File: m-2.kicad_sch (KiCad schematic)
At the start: 57 parts, among them J1 2199230-6, J2 1-2199230-6, M2 M2_4222, M3 M2_2280, U2 74LVC2G07GV, U3 74LVC2G07GV, Y1 ECS-327MVATX-2-CN-TR3

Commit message: Loclib
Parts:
- C10, C13, C14, C15, C16, C17, C18, C19, C20, C9: footprint antmicro-footprints:0402-cap -> jetson-orin-baseboard-footprints:0402-cap; symbol antmicroCapacitors0402:C_220n_0402 -> jetson-orin-baseboard:C_220n_0402
- C11, C12, C21, C22, C23, C24: footprint antmicro-footprints:0603-cap -> jetson-orin-baseboard-footprints:0603-cap; symbol antmicroCapacitors0603:C_10u_0603 -> jetson-orin-baseboard:C_10u_0603
- C25, C7, C8: footprint antmicro-footprints:0402-cap -> jetson-orin-baseboard-footprints:0402-cap; symbol antmicroCapacitors0402:C_100n_0402 -> jetson-orin-baseboard:C_100n_0402
- D1: footprint antmicro-footprints:LED_0603 -> jetson-orin-baseboard-footprints:LED_0603; symbol antmicroLEDIndicationDiscrete:LTST-C190GKT -> jetson-orin-baseboard:LTST-C190GKT
- J1: footprint antmicro-footprints:2199230-4 -> jetson-orin-baseboard-footprints:2199230-4; symbol antmicroPciConnectors:2199230-6 -> jetson-orin-baseboard:2199230-6
- J2: footprint antmicro-footprints:1-2199230-6 -> jetson-orin-baseboard-footprints:1-2199230-6; symbol antmicroPciConnectors:1-2199230-6 -> jetson-orin-baseboard:1-2199230-6
- M2: footprint antmicro-footprints:m2_4222 -> jetson-orin-baseboard-footprints:m2_4222; symbol antmicroModules:M2_4222 -> jetson-orin-baseboard:M2_4222
- M3: footprint antmicro-footprints:m2_2280 -> jetson-orin-baseboard-footprints:m2_2280; symbol antmicroModules:M2_2280 -> jetson-orin-baseboard:M2_2280
- R13, R14, R15, R16, R17, R18, R19, R20, R29, R30, R31, R52: footprint antmicro-footprints:0402-res -> jetson-orin-baseboard-footprints:0402-res; symbol antmicroResistors0402:R_0R_0402 -> jetson-orin-baseboard:R_0R_0402
- R143: footprint antmicro-footprints:0805-res -> jetson-orin-baseboard-footprints:0805-res; symbol antmicroResistorsmisc:R_0R_0805 -> jetson-orin-baseboard:R_0R_0805
- R21, R22: footprint antmicro-footprints:EXB18V -> jetson-orin-baseboard-footprints:EXB18V; symbol antmicroResistorNetworksArrays:4x0R_0201_array -> jetson-orin-baseboard:4x0R_0201_array
- R27, R28, R32, R37, R38: footprint antmicro-footprints:0402-res -> jetson-orin-baseboard-footprints:0402-res; symbol antmicroResistors0402:R_47k_0402 -> jetson-orin-baseboard:R_47k_0402
- R39: footprint antmicro-footprints:0603-res -> jetson-orin-baseboard-footprints:0603-res; symbol antmicroResistors0603:R_330R_0603 -> jetson-orin-baseboard:R_330R_0603
- SP7, SP8: footprint antmicro-footprints:9774025151 -> jetson-orin-baseboard-footprints:9774025151; symbol antmicroMechanicalParts:9774025151 -> jetson-orin-baseboard:9774025151
- TP10, TP11, TP12, TP6, TP7, TP8, TP9: footprint antmicro-footprints:Testpoint_smd_0_75mm -> jetson-orin-baseboard-footprints:Testpoint_smd_0_75mm; symbol antmicroTestPoints:TP_SMD_0_75MM -> jetson-orin-baseboard:TP_SMD_0_75MM
- U2, U3: footprint antmicro-footprints:SC-74 -> jetson-orin-baseboard-footprints:SC-74; symbol antmicroLogicBuffersDriversReceiversTransceivers:74LVC2G07GV -> jetson-orin-baseboard:74LVC2G07GV
- Y1: footprint antmicro-footprints:Oscillator_SMD_ECS_2520MV-xxx-xx-4Pin_2.5x2.0mm -> jetson-orin-baseboard-footprints:Oscillator_SMD_ECS_2520MV-xxx-xx-4Pin_2.5x2.0mm; symbol antmicroOscillators:ECS-327MVATX-2-CN-TR3 -> jetson-orin-baseboard:ECS-327MVATX-2-CN-TR3
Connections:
- net M2_E_UART_CTS: no longer R22.6
- net M2_E_UART_RTS: no longer R22.7
- net M2_E_UART_RX: no longer R22.8
- net M2_E_UART_TX: no longer R22.5
- net UART0_CTS: no longer R22.3
- net UART0_RTS: no longer R22.2
- net UART0_RXD: no longer R22.4
- net UART0_TXD: no longer R22.1

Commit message: Fix symbols after loclib
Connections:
- net M2_E_UART_CTS: now also R22.6
- net M2_E_UART_RTS: now also R22.7
- net M2_E_UART_RX: now also R22.8
- net M2_E_UART_TX: now also R22.5
- net UART0_CTS: now also R22.3
- net UART0_RTS: now also R22.2
- net UART0_RXD: now also R22.4
- net UART0_TXD: now also R22.1

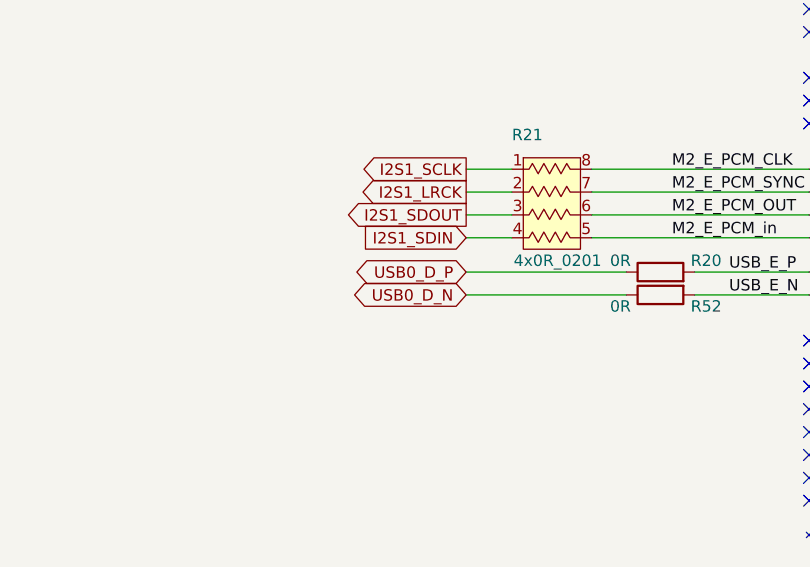
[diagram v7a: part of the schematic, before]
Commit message: Swapped order of USB 2.0 lanes [#40389]
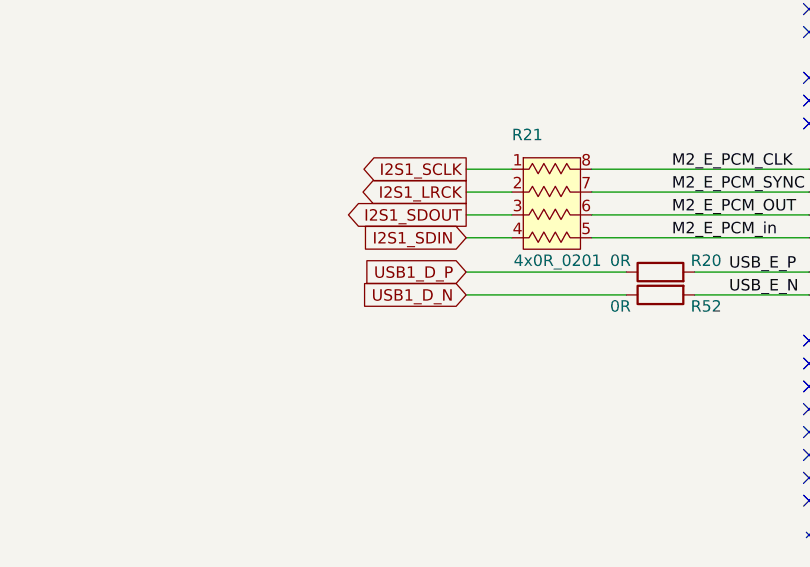
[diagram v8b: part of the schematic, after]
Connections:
- net USB0_D_N renamed USB1_D_N
- net USB0_D_P renamed USB1_D_P
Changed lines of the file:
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@@
+    )
+  )
+  (global_label "USB1_D_P" (shape input) (at 156.21 238.76 180)
+    (effects (font (size 1.27 1.27)) (justify right))
+    (property "Intersheet References" "${INTERSHEET_REFS}" (id 0) (at 140.335 238.76 0)
+      (effects (font (size 1.27 1.27)) (justify right))
     )
   )
@@
     )
   )
+  (global_label "USB1_D_N" (shape input) (at 156.21 241.3 180)
+    (effects (font (size 1.27 1.27)) (justify right))
+    (property "Intersheet References" "${INTERSHEET_REFS}" (id 0) (at 140.335 241.3 0)
+      (effects (font (size 1.27 1.27)) (justify right))
+    )
+  )
   (global_label "PCIE1_CLK_P" (shape input) (at 151.13 171.45 180)
     (effects (font (size 1.27 1.27)) (justify right))
@@
     (property "Intersheet References" "${INTERSHEET_REFS}" (id 0) (at 322.58 186.69 0)
       (effects (font (size 1.27 1.27)) (justify left))
-    )
-  )
-  (global_label "USB0_D_P" (shape bidirectional) (at 156.21 238.76 180)
-    (effects (font (size 1.27 1.27)) (justify right))
-    (property "Intersheet References" "${INTERSHEET_REFS}" (id 0) (at 142.875 238.76 0)
-      (effects (font (size 1.1 1.1)) (justify right))
     )
   )
@@
     )
   )
-  (global_label "USB0_D_N" (shape bidirectional) (at 156.21 241.3 180)
-    (effects (font (size 1.27 1.27)) (justify right))
-    (property "Intersheet References" "${INTERSHEET_REFS}" (id 0) (at 142.875 241.3 0)
-      (effects (font (size 1.1 1.1)) (justify right))
-    )
-  )
